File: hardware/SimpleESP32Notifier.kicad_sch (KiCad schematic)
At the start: 1 part, among them U1 Heltec_HTIT-WB32

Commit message: Decided layout
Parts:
- added D1, D2, D3: LED, LED_THT:LED_D5.0mm, symbol Device:LED
- added R1, R2, R3: 10k, Resistor_THT:R_Axial_DIN0207_L6.3mm_D2.5mm_P7.62mm_Horizontal, symbol Device:R
- added R4, R5, R6: 220, Resistor_THT:R_Axial_DIN0207_L6.3mm_D2.5mm_P7.62mm_Horizontal, symbol Device:R
- added SW1, SW2, SW3: SW_Push, Button_Switch_THT:SW_PUSH_6mm, symbol Switch:SW_Push
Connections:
- net LED_3: now reaches U1.37
- net LED_3: now also R6.1
- net BUT_3: now reaches U1.38
- net BUT_3: now also R3.2, SW3.1
- new net: D1.2 (A), R4.2
- new net: D2.2 (A), R5.2
- new net: D3.2 (A), R6.2
- new net +3.3V: R1.1, R2.1, R3.1
- new net BUT_1: R1.2, SW1.1
- new net BUT_2: R2.2, SW2.1
- new net GND: D1.1 (K), D2.1 (K), D3.1 (K), SW1.2, SW2.2, SW3.2
- new net LED_1: R4.1
- new net LED_2: R5.1
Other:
- moved on the sheet: U1

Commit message: Finished schematic
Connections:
- net +3.3V: now also U1.11 (3.3), U1.9 (3.3)
- net BUT_1: now also U1.12
- net BUT_2: now also U1.33
- net GND: now also U1.28 (GND), U1.8 (GND)
- net LED_1: now also U1.14
- net LED_2: now also U1.32
- no-connect marks 0 -> 26

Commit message: Exported V1.0
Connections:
- net +3.3V: no longer U1.11 (3.3)
- no-connect marks 26 -> 27
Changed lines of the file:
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@@
+	)
+	(no_connect
+		(at 90.17 77.47)
 	)
 	(no_connect
@@
 		(pts
 			(xy 46.99 100.33) (xy 49.53 100.33)
-		)
-		(stroke
-			(width 0)
-			(type default)
-		)
-	)
-	(wire
-		(pts
-			(xy 90.17 77.47) (xy 92.71 77.47)
 		)
 		(stroke
@@
 					(unit 1)
 				)
-			)
-		)
-	)
-	(symbol
-		(lib_id "power:+3.3V")
-		(at 92.71 77.47 270)
-		(unit 1)
-		(exclude_from_sim no)
-		(in_bom yes)
-		(on_board yes)
-		(dnp no)
-		(fields_autoplaced yes)
-		(property "Reference" "#PWR011"
-			(at 88.9 77.47 0)
-			(effects
-				(font
-					(size 1.27 1.27)
-				)
-				(hide yes)
-			)
-		)
-		(property "Value" "+3.3V"
-			(at 96.52 77.4699 90)
-			(effects
-				(font
-					(size 1.27 1.27)
-				)
-				(justify left)
-			)
-		)
-		(property "Footprint" ""
-			(at 92.71 77.47 0)
-			(effects
-				(font
-					(size 1.27 1.27)
-				)
-				(hide yes)
-			)
-		)
-		(property "Datasheet" ""
-			(at 92.71 77.47 0)
-			(effects
-				(font
-					(size 1.27 1.27)
-				)
-				(hide yes)
-			)
-		)
-		(property "Description" "Power symbol creates a global label with name \"+3.3V\""
-			(at 92.71 77.47 0)
-			(effects
-				(font
-					(size 1.27 1.27)
-				)
-				(hide yes)
-			)
-		)
-		(pin "1"
-		)
-		(instances
-			(project "SimpleESP32Notifier"
-				(path "/ceab11b9-b7c1-4693-af6a-2bbcb9d5be0a"
-					(reference "#PWR011")
-					(unit 1)
-				)

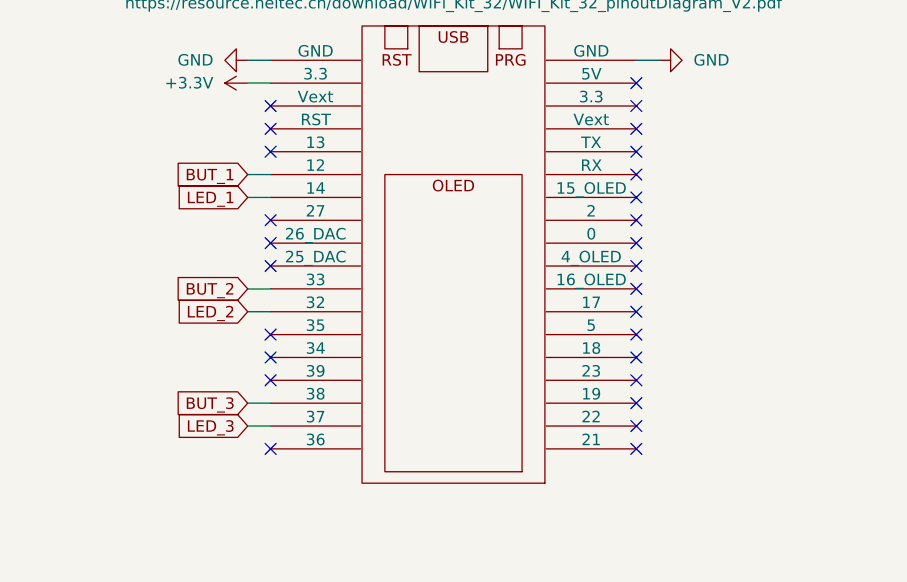
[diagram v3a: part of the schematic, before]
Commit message: Fixed pins wiring of v1.0
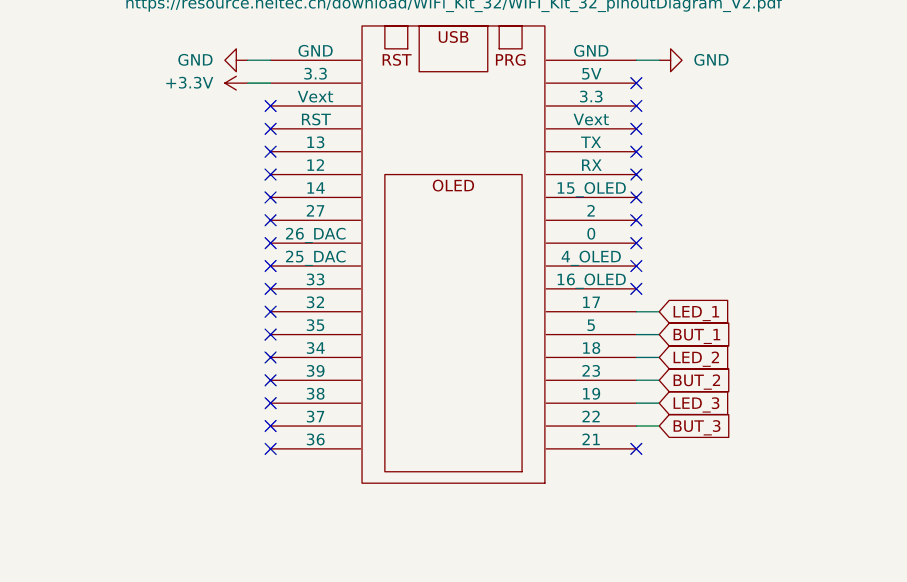
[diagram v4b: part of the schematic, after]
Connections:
- net BUT_1: now also U1.5; no longer U1.12
- net BUT_2: now also U1.23; no longer U1.33
- net BUT_3: now also U1.22; no longer U1.38
- net LED_1: now also U1.17; no longer U1.14
- net LED_2: now also U1.18; no longer U1.32
- net LED_3: now also U1.19; no longer U1.37
